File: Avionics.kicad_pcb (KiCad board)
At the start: 2 copper layers, 321.1 x 96.2 mm, 18 parts

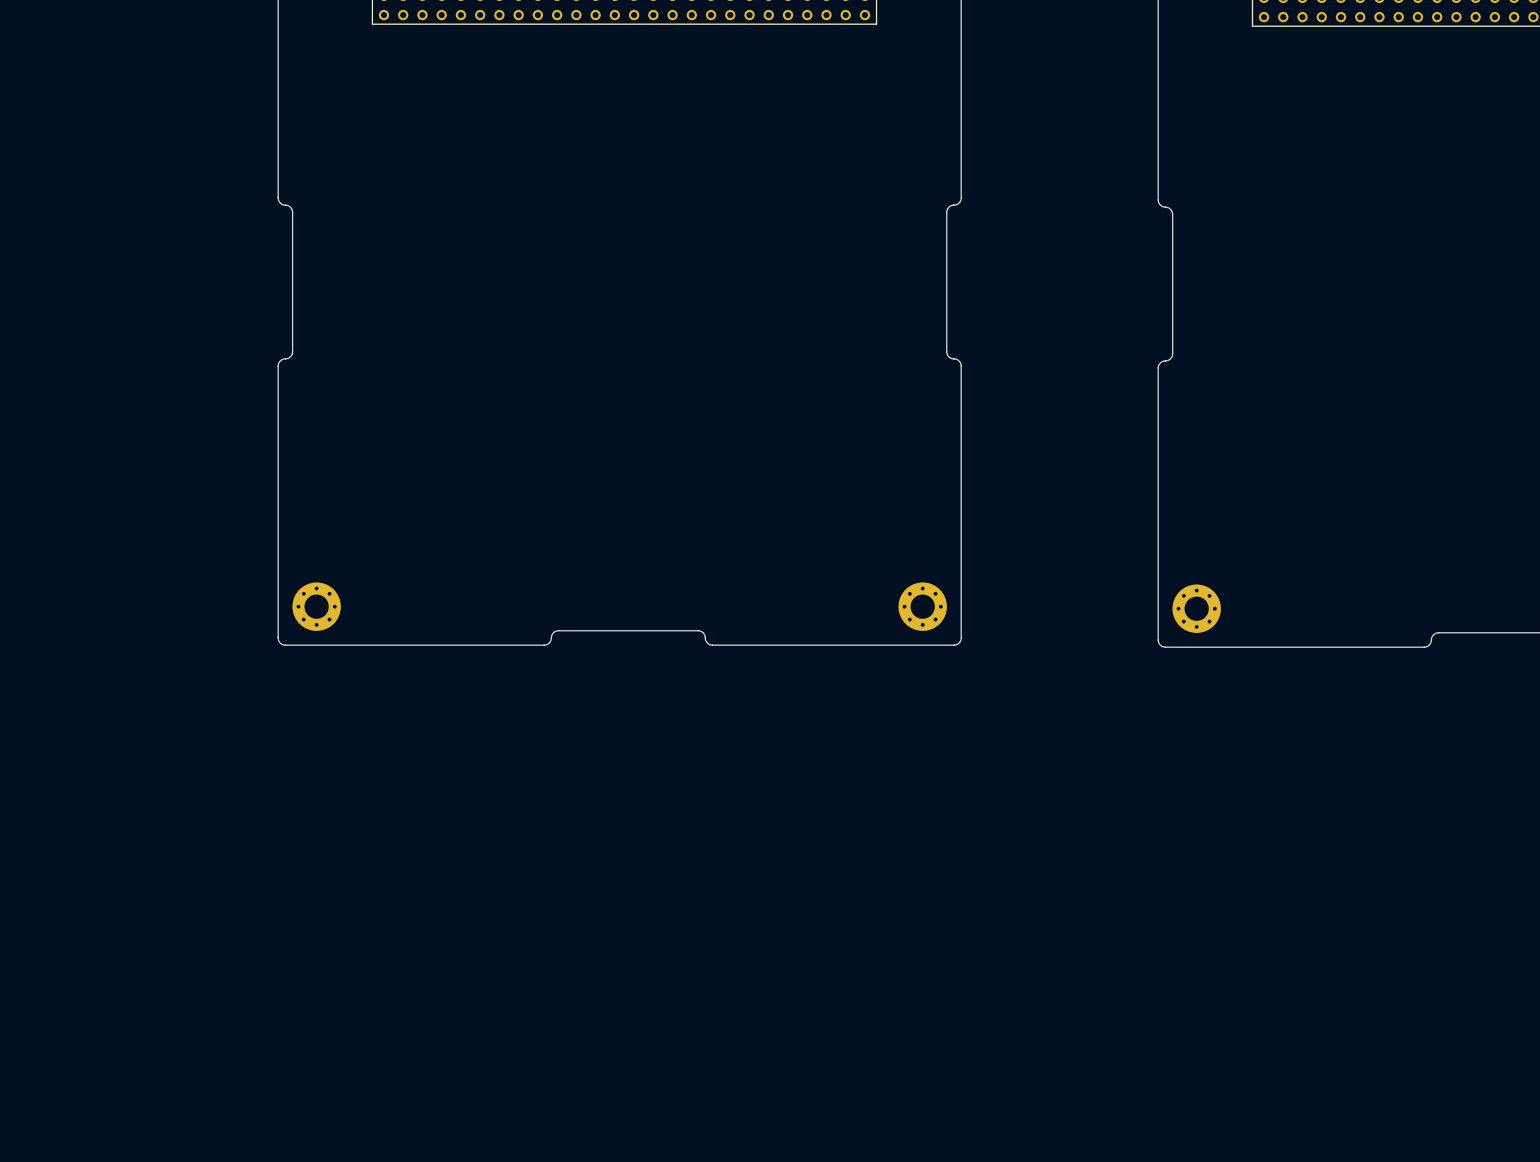
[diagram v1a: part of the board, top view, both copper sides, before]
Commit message: OBC: preliminary layout
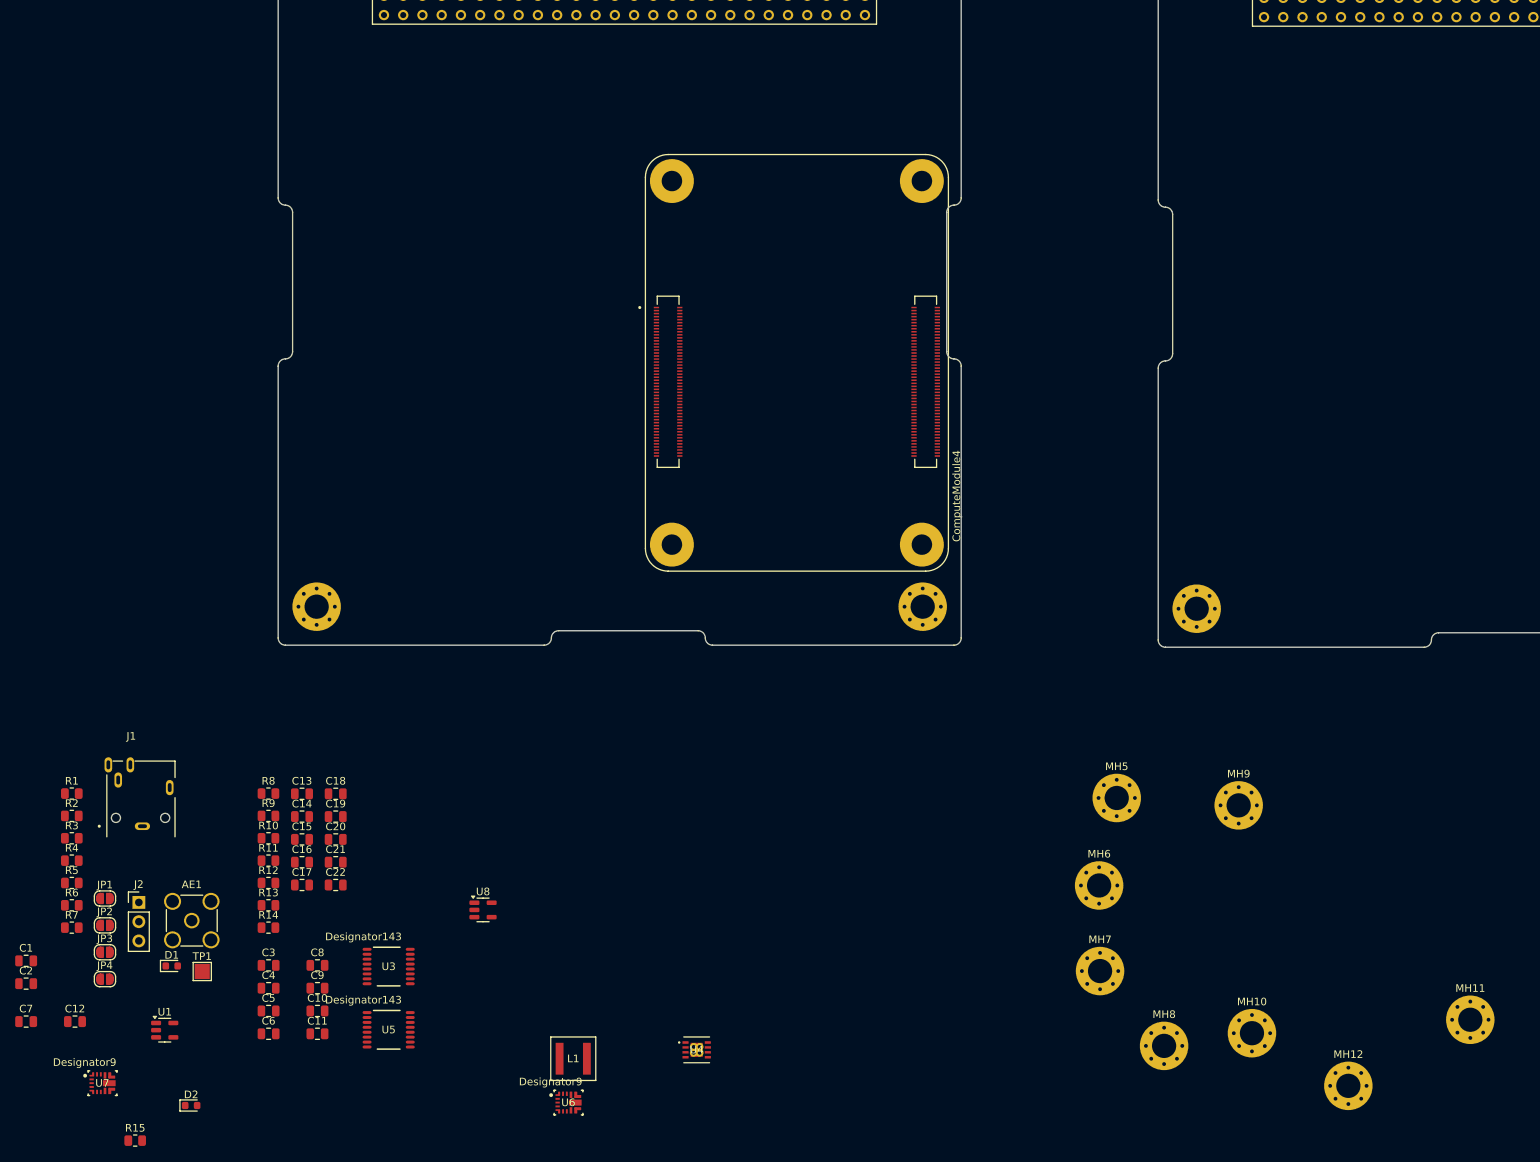
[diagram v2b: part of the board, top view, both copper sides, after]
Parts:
- added AE1: Antenna, Connector_Coaxial:SMA_Amphenol_901-144_Vertical, F.Cu at (45.4, 167.1)
- added C1: 0u1, Capacitor_SMD:C_0805_2012Metric, F.Cu at (23.5, 172.4)
- added C10: 4u7, Capacitor_SMD:C_0805_2012Metric, F.Cu at (62.0, 179.0)
- added C11: 0u1, Capacitor_SMD:C_0805_2012Metric, F.Cu at (62.0, 182.0)
- added C12: 0.1u, Capacitor_SMD:C_0805_2012Metric, F.Cu at (30.0, 180.4)
- added C13: 100u, 35V, Capacitor_SMD:C_0805_2012Metric, F.Cu at (60.0, 150.3)
- added C14: 10u, 25V, 0805, Capacitor_SMD:C_0805_2012Metric, F.Cu at (60.0, 153.4)
- added C15: 10u, 25V, 0805, Capacitor_SMD:C_0805_2012Metric, F.Cu at (60.0, 156.4)
- added C16: 0u1, 50v, 0805, Capacitor_SMD:C_0805_2012Metric, F.Cu at (60.0, 159.4)
- added C17: 0u1, 50v, 0805, Capacitor_SMD:C_0805_2012Metric, F.Cu at (60.0, 162.4)
- added C18: 2u2, 10V, 0805, Capacitor_SMD:C_0805_2012Metric, F.Cu at (64.4, 150.3)
- added C19: 0u1, 50V, 0805, Capacitor_SMD:C_0805_2012Metric, F.Cu at (64.4, 153.4)
- added C2: 0u1, Capacitor_SMD:C_0805_2012Metric, F.Cu at (23.5, 175.4)
- added C20: 33p, Capacitor_SMD:C_0805_2012Metric, F.Cu at (64.4, 156.4)
- added C21: 47u, 10V, 0805, Capacitor_SMD:C_0805_2012Metric, F.Cu at (64.4, 159.4)
- added C22: 47u, 10V, 0805, Capacitor_SMD:C_0805_2012Metric, F.Cu at (64.4, 162.4)
- added C3: 4u7, Capacitor_SMD:C_0805_2012Metric, F.Cu at (55.6, 173.0)
- added C4: 0u1, Capacitor_SMD:C_0805_2012Metric, F.Cu at (55.6, 176.0)
- added C5: 4u7, Capacitor_SMD:C_0805_2012Metric, F.Cu at (55.6, 179.0)
- added C6: 0u1, Capacitor_SMD:C_0805_2012Metric, F.Cu at (55.6, 182.0)
- added C7: 0.1u, Capacitor_SMD:C_0805_2012Metric, F.Cu at (23.5, 180.4)
- added C8: 4u7, Capacitor_SMD:C_0805_2012Metric, F.Cu at (62.0, 173.0)
- added C9: 0u1, Capacitor_SMD:C_0805_2012Metric, F.Cu at (62.0, 176.0)
- added D1: LED RED, LED_SMD:LED_0603_1608Metric, F.Cu at (42.8, 173.1)
- added D2: LED GREEN, LED_SMD:LED_0603_1608Metric, F.Cu at (45.3, 191.5)
- added J1: 54-00175, 54_00175-audio-jack:TENSILITY_54-00175, F.Cu at (38.7, 151.0)
- added J2: Conn_01x03, Connector_PinHeader_2.54mm:PinHeader_1x03_P2.54mm_Vertical, F.Cu at (38.4, 164.7)
- added JP1: ~, Jumper:SolderJumper-2_P1.3mm_Open_RoundedPad1.0x1.5mm, F.Cu at (34.0, 164.2)
- added JP2: ~, Jumper:SolderJumper-2_P1.3mm_Open_RoundedPad1.0x1.5mm, F.Cu at (34.0, 167.7)
- added JP3: ~, Jumper:SolderJumper-2_P1.3mm_Open_RoundedPad1.0x1.5mm, F.Cu at (34.0, 171.3)
- added JP4: ~, Jumper:SolderJumper-2_P1.3mm_Open_RoundedPad1.0x1.5mm, F.Cu at (34.0, 174.8)
- added L1: XGL5050-182MEC, XGL5050-182MEC:IND_XGL5050_COC, F.Cu at (95.8, 185.3)
- added MH10: MountingHole_Pad, MountingHole:MountingHole_3.2mm_M3_Pad_Via, F.Cu at (185.4, 181.9)
- added MH11: MountingHole_Pad, MountingHole:MountingHole_3.2mm_M3_Pad_Via, F.Cu at (214.2, 180.2)
- added MH12: MountingHole_Pad, MountingHole:MountingHole_3.2mm_M3_Pad_Via, F.Cu at (198.1, 188.9)
- added MH5: MountingHole_Pad, MountingHole:MountingHole_3.2mm_M3_Pad_Via, F.Cu at (167.5, 150.9)
- added MH6: MountingHole_Pad, MountingHole:MountingHole_3.2mm_M3_Pad_Via, F.Cu at (165.2, 162.4)
- added MH7: MountingHole_Pad, MountingHole:MountingHole_3.2mm_M3_Pad_Via, F.Cu at (165.3, 173.7)
- added MH8: MountingHole_Pad, MountingHole:MountingHole_3.2mm_M3_Pad_Via, F.Cu at (173.8, 183.6)
- added MH9: MountingHole_Pad, MountingHole:MountingHole_3.2mm_M3_Pad_Via, F.Cu at (183.6, 151.9)
- added Module1: ComputeModule4, CM4102008:MODULE_CM4102008, F.Cu at (125.3, 93.5)
- added R1: 60, Resistor_SMD:R_0805_2012Metric, F.Cu at (29.6, 150.3)
- added R10: 6k04, Resistor_SMD:R_0805_2012Metric, F.Cu at (55.5, 156.2)
- added R11: 11k3, Resistor_SMD:R_0805_2012Metric, F.Cu at (55.5, 159.2)
- added R12: 11k8, Resistor_SMD:R_0805_2012Metric, F.Cu at (55.5, 162.1)
- added R13: 10k, Resistor_SMD:R_0805_2012Metric, F.Cu at (55.5, 165.1)
- added R14: 4k99, Resistor_SMD:R_0805_2012Metric, F.Cu at (55.5, 168.0)
- added R15: 28k, Resistor_SMD:R_0805_2012Metric, F.Cu at (37.9, 196.1)
- added R2: 60, Resistor_SMD:R_0805_2012Metric, F.Cu at (29.6, 153.3)
- added R3: 60, Resistor_SMD:R_0805_2012Metric, F.Cu at (29.6, 156.2)
- added R4: 60, Resistor_SMD:R_0805_2012Metric, F.Cu at (29.6, 159.2)
- added R5: 1k, Resistor_SMD:R_0805_2012Metric, F.Cu at (29.6, 162.1)
- added R6: 1k, Resistor_SMD:R_0805_2012Metric, F.Cu at (29.6, 165.1)
- added R7: 4k7, Resistor_SMD:R_0805_2012Metric, F.Cu at (29.6, 168.0)
- added R8: 4k7, Resistor_SMD:R_0805_2012Metric, F.Cu at (55.5, 150.3)
- added R9: 16k9, Resistor_SMD:R_0805_2012Metric, F.Cu at (55.5, 153.3)
- added TP1: TestPoint, TestPoint:TestPoint_Pad_2.0x2.0mm, F.Cu at (46.8, 173.8)
- added U1: 74LVC1GU04DBV, Package_TO_SOT_SMD:SOT-23-5, F.Cu at (41.8, 181.6)
- added U2: OEM719, Novatel:OEM719, B.Cu at (104.7, 50.1)
- added U3: TCAN1051VDRBRQ1, INA260AIPWR:PW0016A_L, F.Cu at (71.4, 173.1)
- added U4: INA260AIPWR, TCAN1051V:DRB8_TEX, F.Cu at (112.1, 184.2)
- added U5: TCAN1051VDRBRQ1, INA260AIPWR:PW0016A_L, F.Cu at (71.4, 181.5)
- added U6: INA260AIPWR, TPS543320RPYR:RPY0014A-MFG, F.Cu at (95.1, 191.1)
- added U7: TPS543320RPYR, TPS543320RPYR:RPY0014A-MFG, F.Cu at (33.6, 188.5)
- added U8: 74LVC1GU04DBV, Package_TO_SOT_SMD:SOT-23-5, F.Cu at (83.9, 165.7)
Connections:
- H1 pad 1: unconnected-(H1-Pin_1-Pad1) -> /OBC/CAN_A_L (x3)
- H1 pad 13: unconnected-(H1-Pin_13-Pad13) -> /OBC/UART_C_TX (x3)
- H1 pad 15: unconnected-(H1-Pin_15-Pad15) -> /OBC/UART_C_RX (x3)
- H1 pad 2: unconnected-(H1-Pin_2-Pad2) -> /OBC/CAN_B_L (x3)
- H1 pad 22: unconnected-(H1-Pin_22-Pad22) -> /OBC/GPIO8 (x3)
- H1 pad 24: unconnected-(H1-Pin_24-Pad24) -> /OBC/GPIO9 (x3)
- H1 pad 25: unconnected-(H1-Pin_25-Pad25) -> /OBC/5V_PERM (x3)
- H1 pad 26: unconnected-(H1-Pin_26-Pad26) -> /OBC/5V_PERM (x3)
- H1 pad 29: unconnected-(H1-Pin_29-Pad29) -> GND (x3)
- H1 pad 3: unconnected-(H1-Pin_3-Pad3) -> /OBC/CAN_A_H (x3)
- H1 pad 30: unconnected-(H1-Pin_30-Pad30) -> GND (x3)
- H1 pad 31: unconnected-(H1-Pin_31-Pad31) -> GND (x3)
- H1 pad 32: unconnected-(H1-Pin_32-Pad32) -> GND (x3)
- H1 pad 38: unconnected-(H1-Pin_38-Pad38) -> /OBC/GPIO12 (x3)
- H1 pad 4: unconnected-(H1-Pin_4-Pad4) -> /OBC/CAN_B_H (x3)
- H1 pad 40: unconnected-(H1-Pin_40-Pad40) -> /OBC/GPIO13 (x3)
- H1 pad 42: unconnected-(H1-Pin_42-Pad42) -> /OBC/UART_F_TX (x3)
- H1 pad 44: unconnected-(H1-Pin_44-Pad44) -> /OBC/UART_F_RX (x3)
- H1 pad 45: unconnected-(H1-Pin_45-Pad45) -> /OBC/ENA_PWR_1 (x3)
- H1 pad 46: unconnected-(H1-Pin_46-Pad46) -> +5V_MPU (x3)
- H1 pad 47: unconnected-(H1-Pin_47-Pad47) -> /OBC/ENA_PWR_2 (x3)
- H1 pad 48: unconnected-(H1-Pin_48-Pad48) -> +5V_GNSS (x3)
- H1 pad 49: unconnected-(H1-Pin_49-Pad49) -> /OBC/ENA_PWR_3 (x3)
- H1 pad 5: unconnected-(H1-Pin_5-Pad5) -> /OBC/UART_A_TX (x3)
- H1 pad 50: unconnected-(H1-Pin_50-Pad50) -> /OBC/PWR_3 (x3)
- H1 pad 51: unconnected-(H1-Pin_51-Pad51) -> /OBC/ENA_PWR_4 (x3)
- H1 pad 52: unconnected-(H1-Pin_52-Pad52) -> /OBC/PWR_4 (x3)
- H1 pad 6: unconnected-(H1-Pin_6-Pad6) -> /OBC/UART_B_TX (x3)
- H1 pad 7: unconnected-(H1-Pin_7-Pad7) -> /OBC/UART_A_RX (x3)
- H1 pad 8: unconnected-(H1-Pin_8-Pad8) -> /OBC/UART_B_RX (x3)
- H2 pad 25: +5V -> /OBC/5V_PERM (x3)
- H2 pad 26: +5V -> /OBC/5V_PERM (x3)
- H2 pad 27: +3V3 -> unconnected-(H2-Pad27) (x3)
- H2 pad 28: +3V3 -> unconnected-(H2-Pad28) (x3)
- H2 pad 33: unconnected-(H2-Pin_33-Pad33) -> /OBC/ENA_PWR_5 (x3)
- H2 pad 34: unconnected-(H2-Pin_34-Pad34) -> /OBC/PWR_5 (x3)
- H2 pad 35: unconnected-(H2-Pin_35-Pad35) -> /OBC/ENA_PWR_6 (x3)
- H2 pad 36: unconnected-(H2-Pin_36-Pad36) -> /OBC/PWR_6 (x3)
- H2 pad 37: unconnected-(H2-Pin_37-Pad37) -> /OBC/ENA_PWR_7 (x3)
- H2 pad 38: unconnected-(H2-Pin_38-Pad38) -> /OBC/PWR_7 (x3)
- H2 pad 39: unconnected-(H2-Pin_39-Pad39) -> /OBC/ENA_PWR_8 (x3)
- H2 pad 40: unconnected-(H2-Pin_40-Pad40) -> /OBC/PWR_8 (x3)
- H2 pad 43: unconnected-(H2-Pin_43-Pad43) -> /OBC/CHARGE (x3)
- H2 pad 44: unconnected-(H2-Pin_44-Pad44) -> /OBC/CHARGE (x3)
- H2 pad 45: unconnected-(H2-Pin_45-Pad45) -> /OBC/BATT (x3)
- H2 pad 46: unconnected-(H2-Pin_46-Pad46) -> /OBC/BATT (x3)
- H2 pad 47: unconnected-(H2-Pin_47-Pad47) -> /OBC/RBF_A (x3)
- H2 pad 48: unconnected-(H2-Pin_48-Pad48) -> /OBC/DS_A (x3)
- H2 pad 49: unconnected-(H2-Pin_49-Pad49) -> /OBC/RBF_B (x3)
- H2 pad 50: unconnected-(H2-Pin_50-Pad50) -> /OBC/DS_B (x3)
- H2 pad 51: unconnected-(H2-Pin_51-Pad51) -> /OBC/RBF_C (x3)
- H2 pad 52: unconnected-(H2-Pin_52-Pad52) -> /OBC/DS_C (x3)
- MH1 pad 1: unconnected-(MH1-Pad1)_7 -> GND (x3)
- MH2 pad 1: unconnected-(MH2-Pad1)_1 -> GND (x3)
- MH3 pad 1: unconnected-(MH3-Pad1)_6 -> GND (x3)
- MH4 pad 1: unconnected-(MH4-Pad1)_6 -> GND (x3)

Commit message: OBC: start PCB layout
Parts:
- removed J2: Conn_01x03, Connector_PinHeader_2.54mm:PinHeader_1x03_P2.54mm_Vertical
- removed TP1: TestPoint, TestPoint:TestPoint_Pad_2.0x2.0mm
- removed the U1 at (41.8, 181.6)
- removed U8: 74LVC1GU04DBV, Package_TO_SOT_SMD:SOT-23-5
- added JP5: WiFi_nDisable, Jumper:SolderJumper-2_P1.3mm_Open_RoundedPad1.0x1.5mm, B.Cu at (64.7, 109.2)
- added JP6: BT_nDisable, Jumper:SolderJumper-2_P1.3mm_Bridged_RoundedPad1.0x1.5mm, B.Cu at (64.7, 111.7)
- C1, C10, C11, C12, C13, C14, C15, C16, C17, C18, C19, C2, C20, C21, C22, C3, C4, C5, C6, C7, C8, C9, JP1, JP2, JP3, JP4, L1, R1, R10, R11, R12, R13, R14, R15, R2, R3, R4, R7, R8, R9: moved to B.Cu
- D1: renamed from D2; footprint LED_SMD:LED_0603_1608Metric -> LED_SMD:LED_0805_2012Metric
- D2: renamed from D1; footprint LED_SMD:LED_0603_1608Metric -> LED_SMD:LED_0805_2012Metric
- MH1 (x3), MH2 (x3), MH3 (x3), MH4 (x3): footprint VST104_footprints:MountingHole_3.2mm_M3_Pad_Via -> MountingHole:MountingHole_3.2mm_M3_Pad_Via
- R5: renamed from R6; value 1k -> 39
- R6: renamed from R5; value 1k -> 45
- U2: renamed from U3; footprint INA260AIPWR:PW0016A_L -> TCAN1051V:DRB8_TEX; moved to B.Cu
- U3: renamed from U4; footprint TCAN1051V:DRB8_TEX -> INA260AIPWR:PW0016A_L; moved to B.Cu
- U4: renamed from U5; footprint INA260AIPWR:PW0016A_L -> TCAN1051V:DRB8_TEX; moved to B.Cu
- U5: renamed from U6; footprint TPS543320RPYR:RPY0014A-MFG -> INA260AIPWR:PW0016A_L; moved to B.Cu
- U6: renamed from U7; moved to B.Cu
- moved MH6 246.3 mm to (408.8, 198.7)
- moved MH7 245.4 mm to (408.8, 204.1)
- moved MH5 244.1 mm to (408.8, 187.8)
- moved MH8 237.9 mm to (408.8, 220.4)
- moved MH9 228.9 mm to (408.8, 193.2)
- moved MH10 225.9 mm to (408.8, 214.9)
- moved MH12 213.9 mm to (408.8, 225.8)
- moved MH11 196.8 mm to (408.8, 209.5)
- moved C7 164.2 mm to (139.7, 64.4), turned to -90 degrees
- moved U6 148.0 mm to (116.0, 65.6), turned to 180 degrees
- moved R15 142.9 mm to (108.9, 72.1), turned to 180 degrees
- moved C2 139.8 mm to (88.1, 51.4)
- moved JP4 129.8 mm to (85.5, 55.7), turned to 180 degrees
- moved JP3 128.0 mm to (88.9, 55.7), turned to 180 degrees
- moved C6 125.1 mm to (83.6, 60.2), turned to 180 degrees
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- renumbered U2 to U1
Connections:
- net /OBC/+1.8v renamed Net-(Module1A-+1.8v_(Output)-Pad88)
- net /OBC/GPIO11 renamed /OBC/GNSS_NRESET_IN
- net /OBC/GPIO12 renamed /OBC/UART_DATA_TX
- net /OBC/GPIO13 renamed /OBC/UART_DATA_RX
- net /OBC/GPIO17 renamed /OBC/GNSS_PV
- net /OBC/GPIO22 renamed /OBC/GNSS_PPS
- net /OBC/GPIO8 renamed /OBC/UART_COMM_TX
- net /OBC/GPIO9 renamed /OBC/UART_COMM_RX
- AE1 pad 1: unconnected-(AE1-A-Pad1) -> Net-(AE1-A)
- C3 pad 1: +5V -> +5V_CM4
- C4 pad 1: +5V -> +5V_CM4
- C8 pad 1: +5V -> +5V_CM4
- C9 pad 1: +5V -> +5V_CM4
- D1 pad 1: Net-(D2-K) -> GND
- D1 pad 2: +3V3 -> Net-(D1-A)
- D2 pad 1: Net-(D1-K) -> GND
- D2 pad 2: +3V3 -> Net-(D2-A)
- JP3 pad 2: /OBC/CAN_A_H -> /OBC/CAN_B_H
- JP4 pad 1: /OBC/CAN_A_L -> /OBC/CAN_B_L
- Module1 pad 10: /OBC/TRD0_N -> unconnected-(Module1A-Ethernet_Pair0_N-Pad10)
- Module1 pad 11: /OBC/TRD2_P -> unconnected-(Module1A-Ethernet_Pair2_P-Pad11)
- Module1 pad 115: /OBC/CAM1_D0_N -> unconnected-(Module1B-CAM1_D0_N-Pad115)
- Module1 pad 117: /OBC/CAM1_D0_P -> unconnected-(Module1B-CAM1_D0_P-Pad117)
- Module1 pad 12: /OBC/TRD0_P -> unconnected-(Module1A-Ethernet_Pair0_P-Pad12)
- Module1 pad 121: /OBC/CAM1_D1_N -> unconnected-(Module1B-CAM1_D1_N-Pad121)
- Module1 pad 123: /OBC/CAM1_D1_P -> unconnected-(Module1B-CAM1_D1_P-Pad123)
- Module1 pad 127: /OBC/CAM1_C_N -> unconnected-(Module1B-CAM1_C_N-Pad127)
- Module1 pad 128: /OBC/CAM0_D0_N -> unconnected-(Module1B-CAM0_D0_N-Pad128)
- Module1 pad 129: /OBC/CAM1_C_P -> unconnected-(Module1B-CAM1_C_P-Pad129)
- Module1 pad 130: /OBC/CAM0_D0_P -> unconnected-(Module1B-CAM0_D0_P-Pad130)
- Module1 pad 133: /OBC/CAM1_D2_N -> unconnected-(Module1B-CAM1_D2_N-Pad133)
- Module1 pad 134: /OBC/CAM0_D1_N -> unconnected-(Module1B-CAM0_D1_N-Pad134)
- Module1 pad 135: /OBC/CAM1_D2_P -> unconnected-(Module1B-CAM1_D2_P-Pad135)
- Module1 pad 136: /OBC/CAM0_D1_P -> unconnected-(Module1B-CAM0_D1_P-Pad136)
- Module1 pad 139: /OBC/CAM1_D3_N -> unconnected-(Module1B-CAM1_D3_N-Pad139)
- Module1 pad 140: /OBC/CAM0_C_N -> unconnected-(Module1B-CAM0_C_N-Pad140)
- Module1 pad 141: /OBC/CAM1_D3_P -> unconnected-(Module1B-CAM1_D3_P-Pad141)
- Module1 pad 142: /OBC/CAM0_C_P -> unconnected-(Module1B-CAM0_C_P-Pad142)
- Module1 pad 143: /OBC/HDMI1_HOTPLUG -> unconnected-(Module1B-HDMI1_HOTPLUG-Pad143)
- Module1 pad 145: /OBC/HDMI1_SDA -> unconnected-(Module1B-HDMI1_SDA-Pad145)
- Module1 pad 146: /OBC/HDMI1_D2_P -> unconnected-(Module1B-HDMI1_TX2_P-Pad146)
- Module1 pad 147: /OBC/HDMI1_SCL -> unconnected-(Module1B-HDMI1_SCL-Pad147)
- Module1 pad 148: /OBC/HDMI1_D2_N -> unconnected-(Module1B-HDMI1_TX2_N-Pad148)
- Module1 pad 149: /OBC/HDMI1_CEC -> unconnected-(Module1B-HDMI1_CEC-Pad149)
- Module1 pad 15: /OBC/ETH_LEDY -> unconnected-(Module1A-Ethernet_nLED3(3.3v)-Pad15)
- Module1 pad 151: /OBC/HDMI0_CEC -> unconnected-(Module1B-HDMI0_CEC-Pad151)
- Module1 pad 152: /OBC/HDMI1_D1_P -> unconnected-(Module1B-HDMI1_TX1_P-Pad152)
- Module1 pad 153: /OBC/HDMI0_HOTPLUG -> unconnected-(Module1B-HDMI0_HOTPLUG-Pad153)
- Module1 pad 154: /OBC/HDMI1_D1_N -> unconnected-(Module1B-HDMI1_TX1_N-Pad154)
- Module1 pad 157: /OBC/DSI0_D0_N -> unconnected-(Module1B-DSI0_D0_N-Pad157)
- Module1 pad 158: /OBC/HDMI1_D0_P -> unconnected-(Module1B-HDMI1_TX0_P-Pad158)
- Module1 pad 159: /OBC/DSI0_D0_P -> unconnected-(Module1B-DSI0_D0_P-Pad159)
- Module1 pad 16: /OBC/SYNC_IN -> unconnected-(Module1A-Ethernet_SYNC_IN(1.8v)-Pad16)
- Module1 pad 160: /OBC/HDMI1_D0_N -> unconnected-(Module1B-HDMI1_TX0_N-Pad160)
- Module1 pad 163: /OBC/DSI0_D1_N -> unconnected-(Module1B-DSI0_D1_N-Pad163)
- Module1 pad 164: /OBC/HDMI1_CK_P -> unconnected-(Module1B-HDMI1_CLK_P-Pad164)
- Module1 pad 165: /OBC/DSI0_D1_P -> unconnected-(Module1B-DSI0_D1_P-Pad165)
- Module1 pad 166: /OBC/HDMI1_CK_N -> unconnected-(Module1B-HDMI1_CLK_N-Pad166)
- Module1 pad 169: /OBC/DSI0_C_N -> unconnected-(Module1B-DSI0_C_N-Pad169)
- Module1 pad 17: /OBC/ETH_LEDG -> unconnected-(Module1A-Ethernet_nLED2(3.3v)-Pad17)
- Module1 pad 170: /OBC/HDMI0_D2_P -> unconnected-(Module1B-HDMI0_TX2_P-Pad170)
- Module1 pad 171: /OBC/DSI0_C_P -> unconnected-(Module1B-DSI0_C_P-Pad171)
- Module1 pad 172: /OBC/HDMI0_D2_N -> unconnected-(Module1B-HDMI0_TX2_N-Pad172)
- Module1 pad 175: /OBC/DSI1_D0_N -> unconnected-(Module1B-DSI1_D0_N-Pad175)
- Module1 pad 176: /OBC/HDMI0_D1_P -> unconnected-(Module1B-HDMI0_TX1_P-Pad176)
- Module1 pad 177: /OBC/DSI1_D0_P -> unconnected-(Module1B-DSI1_D0_P-Pad177)
- Module1 pad 178: /OBC/HDMI0_D1_N -> unconnected-(Module1B-HDMI0_TX1_N-Pad178)
- Module1 pad 18: /OBC/SYNC_OUT -> unconnected-(Module1A-Ethernet_SYNC_OUT(1.8v)-Pad18)
- Module1 pad 181: /OBC/DSI1_D1_N -> unconnected-(Module1B-DSI1_D1_N-Pad181)
- Module1 pad 182: /OBC/HDMI0_D0_P -> unconnected-(Module1B-HDMI0_TX0_P-Pad182)
- Module1 pad 183: /OBC/DSI1_D1_P -> unconnected-(Module1B-DSI1_D1_P-Pad183)
- Module1 pad 184: /OBC/HDMI0_D0_N -> unconnected-(Module1B-HDMI0_TX0_N-Pad184)
- Module1 pad 187: /OBC/DSI1_C_N -> unconnected-(Module1B-DSI1_C_N-Pad187)
- Module1 pad 188: /OBC/HDMI0_CK_P -> unconnected-(Module1B-HDMI0_CLK_P-Pad188)
- Module1 pad 189: /OBC/DSI1_C_P -> unconnected-(Module1B-DSI1_C_P-Pad189)
- Module1 pad 190: /OBC/HDMI0_CK_N -> unconnected-(Module1B-HDMI0_CLK_N-Pad190)
- Module1 pad 193: /OBC/DSI1_D2_N -> unconnected-(Module1B-DSI1_D2_N-Pad193)
- Module1 pad 194: /OBC/DSI1_D3_N -> unconnected-(Module1B-DSI1_D3_N-Pad194)
- Module1 pad 195: /OBC/DSI1_D2_P -> unconnected-(Module1B-DSI1_D2_P-Pad195)
- Module1 pad 196: /OBC/DSI1_D3_P -> unconnected-(Module1B-DSI1_D3_P-Pad196)
- Module1 pad 199: /OBC/HDMI0_SDA -> unconnected-(Module1B-HDMI0_SDA-Pad199)
- Module1 pad 20: /OBC/EEPROM_nWP -> unconnected-(Module1A-EEPROM_nWP-Pad20)
- Module1 pad 200: /OBC/HDMI0_SCL -> unconnected-(Module1B-HDMI0_SCL-Pad200)
- Module1 pad 24: /OBC/GPIO26 -> unconnected-(Module1A-GPIO26-Pad24)
- Module1 pad 25: /OBC/GPIO21 -> unconnected-(Module1A-GPIO21-Pad25)
- Module1 pad 26: /OBC/GPIO19 -> unconnected-(Module1A-GPIO19-Pad26)
- Module1 pad 27: /OBC/GPIO20 -> unconnected-(Module1A-GPIO20-Pad27)
- Module1 pad 3: /OBC/TRD3_P -> unconnected-(Module1A-Ethernet_Pair3_P-Pad3)
- Module1 pad 30: /OBC/GPIO6 -> unconnected-(Module1A-GPIO6-Pad30)
- Module1 pad 37: /OBC/GPIO7 -> unconnected-(Module1A-GPIO7-Pad37)
- Module1 pad 4: /OBC/TRD1_P -> unconnected-(Module1A-Ethernet_Pair1_P-Pad4)
- Module1 pad 41: /OBC/GPIO25 -> unconnected-(Module1A-GPIO25-Pad41)
- Module1 pad 44: /OBC/GPIO10 -> unconnected-(Module1A-GPIO10-Pad44)
- Module1 pad 45: /OBC/GPIO24 -> unconnected-(Module1A-GPIO24-Pad45)
- Module1 pad 47: /OBC/GPIO23 -> unconnected-(Module1A-GPIO23-Pad47)
- Module1 pad 48: /OBC/GPIO27 -> unconnected-(Module1A-GPIO27-Pad48)
- Module1 pad 49: /OBC/GPIO18 -> unconnected-(Module1A-GPIO18-Pad49)
- Module1 pad 5: /OBC/TRD3_N -> unconnected-(Module1A-Ethernet_Pair3_N-Pad5)
- Module1 pad 56: /OBC/GPIO3 -> unconnected-(Module1A-GPIO3-Pad56)
- Module1 pad 57: /OBC/SD_CLK -> unconnected-(Module1A-SD_CLK-Pad57)
- Module1 pad 6: /OBC/TRD1_N -> unconnected-(Module1A-Ethernet_Pair1_N-Pad6)
- Module1 pad 61: /OBC/SD_DAT3 -> unconnected-(Module1A-SD_DAT3-Pad61)
- Module1 pad 62: /OBC/SD_CMD -> unconnected-(Module1A-SD_CMD-Pad62)
- Module1 pad 63: /OBC/SD_DAT0 -> unconnected-(Module1A-SD_DAT0-Pad63)
- Module1 pad 67: /OBC/SD_DAT1 -> unconnected-(Module1A-SD_DAT1-Pad67)
- Module1 pad 69: /OBC/SD_DAT2 -> unconnected-(Module1A-SD_DAT2-Pad69)
- Module1 pad 75: /OBC/SD_PWR_ON -> unconnected-(Module1A-SD_PWR_ON-Pad75)
- Module1 pad 76: /OBC/Reserved -> unconnected-(Module1A-Reserved-Pad76)
- Module1 pad 77: /OBC/+5V_CM4 -> +5V_CM4
- Module1 pad 79: unconnected-(Module1A-+5v_(Input)-Pad79) -> +5V_CM4
- Module1 pad 81: unconnected-(Module1A-+5v_(Input)-Pad81) -> +5V_CM4
- Module1 pad 83: unconnected-(Module1A-+5v_(Input)-Pad83) -> +5V_CM4
- Module1 pad 85: unconnected-(Module1A-+5v_(Input)-Pad85) -> +5V_CM4
- Module1 pad 87: /OBC/+5V_CM4 -> +5V_CM4
- Module1 pad 89: /OBC/WL_nDis -> Net-(JP5-B)
- Module1 pad 9: /OBC/TRD2_N -> unconnected-(Module1A-Ethernet_Pair2_N-Pad9)
- Module1 pad 91: /OBC/BT_nDis -> Net-(JP6-A)
- Module1 pad 92: /OBC/RUN_PG -> unconnected-(Module1A-RUN_PG-Pad92)
- Module1 pad 93: /OBC/nCM4BOOT -> unconnected-(Module1A-nRPIBOOT-Pad93)
- Module1 pad 94: /OBC/AIN1 -> unconnected-(Module1A-AnalogIP0-Pad94)
- Module1 pad 96: /OBC/AIN0 -> unconnected-(Module1A-AnalogIP1-Pad96)
- Module1 pad 99: /OBC/GLOBAL_EN -> unconnected-(Module1A-Global_EN-Pad99)
- Module1 pad SH1: (no net) -> GND
- Module1 pad SH2: (no net) -> GND
- Module1 pad SH3: (no net) -> GND
- Module1 pad SH4: (no net) -> GND
- R5 pad 1: Net-(R6-Pad1) -> /OBC/PI_nLED_Activity
- R5 pad 2: Net-(D2-K) -> Net-(D1-A)
- R6 pad 1: Net-(R5-Pad1) -> /OBC/nPWR_LED
- R6 pad 2: Net-(D1-K) -> Net-(D2-A)
- U1 pad 1: (no net) -> GND
- U1 pad 2: (no net) -> GND
- U1 pad 3: (no net) -> GND
- U1 pad 4: (no net) -> GND
- U2 pad 3: +5V -> +5V_CM4
- U4 pad 3: +5V -> +5V_CM4
- U5 pad 14: /OBC/+5V_CM4 -> +5V_CM4
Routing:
- net GND: track 0.00 -> 81.2 mm, vias 0 -> 35
- net /OBC/CAN_A_L: track 0.00 -> 28.8 mm, vias 0 -> 1
- net /OBC/CAN_A_H: track 0.00 -> 28.0 mm, vias 0 -> 1
- net /OBC/CAN_B_L: track 0.00 -> 27.7 mm, vias 0 -> 1
- net /OBC/CAN_B_H: track 0.00 -> 25.6 mm, vias 0 -> 1
- net Net-(U6-EN): track 0.00 -> 17.6 mm, vias 0 -> 2
- net +3V3: track 0.00 -> 16.8 mm, vias 0 -> 2
- net +5V_CM4: track 0.00 -> 14.4 mm, vias 0 -> 8
- net Net-(JP6-A): track 0.00 -> 9.75 mm, vias 0 -> 1
- net Net-(U6-FB): track 0.00 -> 9.32 mm, vias 0 -> 2
- net Net-(U6-SYNC_FSEL): track 0.00 -> 7.82 mm, vias 0 -> 2
- net Net-(JP5-B): track 0.00 -> 7.70 mm, vias 0 -> 1
- net +5V_GNSS: track 0.00 -> 7.04 mm, vias 0 -> 1
- net Net-(U6-BP5): track 0.00 -> 6.41 mm
- net Net-(C2-Pad1): track 0.00 -> 4.68 mm
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- added copper zone on F.Cu, net +5V_CM4
- added copper zone on In2.Cu, net +5V_CM4
- added copper zone on B.Cu, net +5V_GNSS
- added copper zone on In1.Cu, net +5V_GNSS
- added copper zone on B.Cu, net /OBC/INA260_OEM719/LOAD
- added copper zone on B.Cu, net /OBC/TPS543320/VOUT
- added copper zone on B.Cu, net GND
- added copper zone on F.Cu, net GND
- added copper zone on B.Cu, net Net-(L1-Pad1)
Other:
- copper layers 2 -> 4
- board text added: "ACTIVITY"
- board text added: "POWER"
